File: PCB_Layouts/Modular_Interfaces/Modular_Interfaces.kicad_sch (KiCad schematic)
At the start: 38 parts, among them J1 RJ45_LED, J10 Conn_01x10_Socket, J11 Conn_01x03_Socket, J12 Conn_01x10_Socket, J13 Conn_01x10_Socket, J14 Conn_01x04_Socket, J15 Conn_01x10_Socket, J16 Conn_01x10_Socket, J2 Conn_01x10_Socket, J3 Conn_01x10_Socket, J4 USB_A, J5 Conn_01x10_Socket, J6 Conn_01x10_Socket, J7 USB_A, J8 USB_A, J9 Conn_01x10_Socket, U1 ENC28J60x-SS, Y1 25MHz

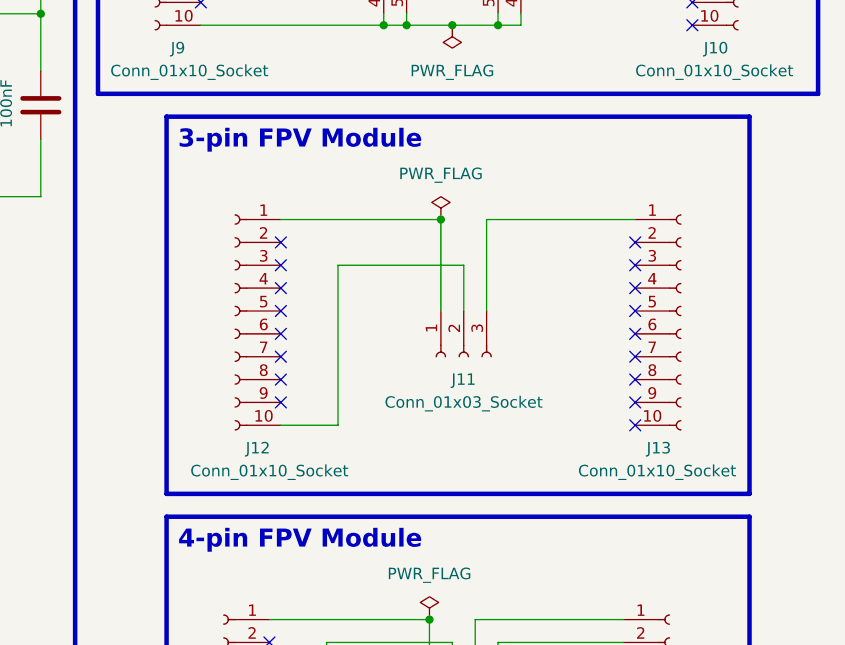
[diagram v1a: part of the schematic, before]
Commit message: Adding Modular Interfaces No GigE module and quote
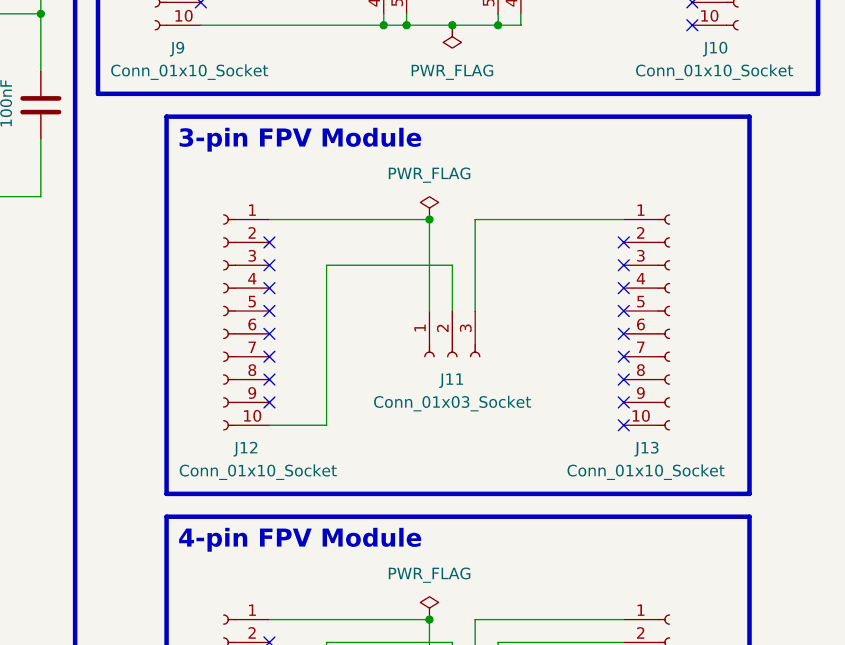
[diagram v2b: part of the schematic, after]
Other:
- title: Modular Interface for Bitcraze Crazyflie 2.0 -> Modular Interfaces for Bitcraze Crazyflie 2.0
- moved on the sheet: J11, J12, J13
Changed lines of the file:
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@@
   (paper "User" 262.992 227.99)
   (title_block
-    (title "Modular Interface for Bitcraze Crazyflie 2.0")
+    (title "Modular Interfaces for Bitcraze Crazyflie 2.0")
     (date "2023-10-04")
     (company "Jose Ignacio Granados Marín")
@@
   (junction (at 24.13 83.82) (diameter 0) (color 0 0 0 0)
   )
-  (junction (at 207.01 106.68) (diameter 0) (color 0 0 0 0)
+  (junction (at 205.74 106.68) (diameter 0) (color 0 0 0 0)
   )
   (junction (at 142.24 104.14) (diameter 0) (color 0 0 0 0)
@@
   )
   (no_connect (at 227.33 173.99))
-  (no_connect (at 228.6 129.54))
+  (no_connect (at 227.33 129.54))
   (no_connect (at 68.58 44.45))
   (no_connect (at 187.96 171.45))
   (no_connect (at 76.2 168.91))
   (no_connect (at 227.33 171.45))
-  (no_connect (at 189.23 124.46))
+  (no_connect (at 187.96 124.46))
   (no_connect (at 187.96 39.37))
   (no_connect (at 227.33 39.37))
-  (no_connect (at 228.6 121.92))
+  (no_connect (at 227.33 121.92))
   (no_connect (at 68.58 34.29))
   (no_connect (at 48.26 24.13))
   (no_connect (at 180.34 80.01))
   (no_connect (at 227.33 41.91))
-  (no_connect (at 189.23 114.3))
-  (no_connect (at 228.6 114.3))
+  (no_connect (at 187.96 114.3))
+  (no_connect (at 227.33 114.3))
   (no_connect (at 68.58 39.37))
   (no_connect (at 187.96 168.91))
   (no_connect (at 227.33 29.21))
   (no_connect (at 234.95 74.93))
-  (no_connect (at 228.6 109.22))
+  (no_connect (at 227.33 109.22))
   (no_connect (at 180.34 69.85))
   (no_connect (at 187.96 153.67))
@@
   (no_connect (at 68.58 104.14))
   (no_connect (at 187.96 41.91))
-  (no_connect (at 189.23 127))
+  (no_connect (at 187.96 127))
   (no_connect (at 76.2 161.29))
   (no_connect (at 234.95 85.09))
@@
   (no_connect (at 227.33 163.83))
   (no_connect (at 68.58 24.13))
-  (no_connect (at 189.23 116.84))
+  (no_connect (at 187.96 116.84))
   (no_connect (at 76.2 166.37))
   (no_connect (at 234.95 77.47))
@@
   (no_connect (at 227.33 36.83))
   (no_connect (at 234.95 67.31))
-  (no_connect (at 228.6 127))
+  (no_connect (at 227.33 127))
   (no_connect (at 68.58 83.82))
   (no_connect (at 227.33 31.75))
-  (no_connect (at 228.6 124.46))
+  (no_connect (at 227.33 124.46))
   (no_connect (at 48.26 41.91))
   (no_connect (at 227.33 26.67))
   (no_connect (at 187.96 24.13))
   (no_connect (at 227.33 44.45))
-  (no_connect (at 228.6 119.38))
+  (no_connect (at 227.33 119.38))
   (no_connect (at 180.34 77.47))
   (no_connect (at 187.96 163.83))
@@
   (no_connect (at 187.96 29.21))
   (no_connect (at 187.96 161.29))
-  (no_connect (at 228.6 116.84))
+  (no_connect (at 227.33 116.84))
   (no_connect (at 187.96 36.83))
-  (no_connect (at 189.23 111.76))
+  (no_connect (at 187.96 111.76))
   (no_connect (at 180.34 72.39))
   (no_connect (at 68.58 36.83))
   (no_connect (at 227.33 161.29))
-  (no_connect (at 189.23 119.38))
-  (no_connect (at 228.6 111.76))
+  (no_connect (at 187.96 119.38))
+  (no_connect (at 227.33 111.76))
   (no_connect (at 68.58 21.59))
   (no_connect (at 187.96 26.67))
@@
   (no_connect (at 180.34 82.55))
   (no_connect (at 187.96 34.29))
-  (no_connect (at 189.23 109.22))
-  (no_connect (at 189.23 121.92))
+  (no_connect (at 187.96 109.22))
+  (no_connect (at 187.96 121.92))
   (no_connect (at 48.26 31.75))
   (no_connect (at 227.33 156.21))
@@
     (stroke (width 0) (type default))
   )
-  (wire (pts (xy 207.01 106.68) (xy 189.23 106.68))
+  (wire (pts (xy 205.74 106.68) (xy 187.96 106.68))
     (stroke (width 0) (type default))
   )
@@
     (stroke (width 0) (type default))
   )
-  (wire (pts (xy 212.09 106.68) (xy 228.6 106.68))
+  (wire (pts (xy 210.82 106.68) (xy 227.33 106.68))
     (stroke (width 0) (type default))
   )
@@
     (stroke (width 0) (type default))
   )
-  (wire (pts (xy 195.58 129.54) (xy 189.23 129.54))
+  (wire (pts (xy 194.31 129.54) (xy 187.96 129.54))
     (stroke (width 0) (type default))
   )
@@
     (stroke (width 0) (type default))
   )
-  (wire (pts (xy 207.01 116.84) (xy 207.01 106.68))
+  (wire (pts (xy 205.74 116.84) (xy 205.74 106.68))
     (stroke (width 0) (type default))
   )
@@
     (stroke (width 0) (type default))
   )
-  (wire (pts (xy 212.09 116.84) (xy 212.09 106.68))
+  (wire (pts (xy 210.82 116.84) (xy 210.82 106.68))
     (stroke (width 0) (type default))
   )
@@
     (stroke (width 0) (type default))
   )
-  (wire (pts (xy 209.55 116.84) (xy 209.55 111.76))
+  (wire (pts (xy 208.28 116.84) (xy 208.28 111.76))
     (stroke (width 0) (type default))
   )
@@
     (stroke (width 0) (type default))
   )
-  (wire (pts (xy 209.55 111.76) (xy 195.58 111.76))
+  (wire (pts (xy 208.28 111.76) (xy 194.31 111.76))
     (stroke (width 0) (type default))
   )
@@
     (stroke (width 0) (type default))
   )
-  (wire (pts (xy 195.58 111.76) (xy 195.58 129.54))
+  (wire (pts (xy 194.31 111.76) (xy 194.31 129.54))
     (stroke (width 0) (type default))
   )
@@
     )
   )
-  (symbol (lib_id "Connector:Conn_01x03_Socket") (at 209.55 121.92 90) (mirror x) (unit 1)
-    (in_bom yes) (on_board yes) (dnp no)
-    (property "Reference" "J11" (at 209.55 124.46 90)
-      (effects (font (size 1.27 1.27)))
-    )
-    (property "Value" "Conn_01x03_Socket" (at 209.55 127 90)
-      (effects (font (size 1.27 1.27)))
-    )
-    (property "Footprint" "Connector_JST:JST_XH_B3B-XH-A_1x03_P2.50mm_Vertical" (at 209.55 121.92 0)
-      (effects (font (size 1.27 1.27)) hide)
-    )
-    (property "Datasheet" "~" (at 209.55 121.92 0)
+  (symbol (lib_id "Connector:Conn_01x03_Socket") (at 208.28 121.92 90) (mirror x) (unit 1)
+    (in_bom yes) (on_board yes) (dnp no)
+    (property "Reference" "J11" (at 208.28 124.46 90)
+      (effects (font (size 1.27 1.27)))
+    )
+    (property "Value" "Conn_01x03_Socket" (at 208.28 127 90)
+      (effects (font (size 1.27 1.27)))
+    )
+    (property "Footprint" "Connector_JST:JST_XH_B3B-XH-A_1x03_P2.50mm_Vertical" (at 208.28 121.92 0)
+      (effects (font (size 1.27 1.27)) hide)
+    )
+    (property "Datasheet" "~" (at 208.28 121.92 0)
       (effects (font (size 1.27 1.27)) hide)
     )
@@
     )
   )
-  (symbol (lib_id "Connector:Conn_01x10_Socket") (at 184.15 116.84 0) (mirror y) (unit 1)
-    (in_bom yes) (on_board yes) (dnp no)
-    (property "Reference" "J12" (at 186.69 132.08 0)
-      (effects (font (size 1.27 1.27)))
-    )
-    (property "Value" "Conn_01x10_Socket" (at 187.96 134.62 0)
-      (effects (font (size 1.27 1.27)))
-    )
-    (property "Footprint" "Connector_PinSocket_2.00mm:PinSocket_1x10_P2.00mm_Vertical" (at 184.15 116.84 0)
-      (effects (font (size 1.27 1.27)) hide)
-    )
-    (property "Datasheet" "~" (at 184.15 116.84 0)
+  (symbol (lib_id "Connector:Conn_01x10_Socket") (at 182.88 116.84 0) (mirror y) (unit 1)
+    (in_bom yes) (on_board yes) (dnp no)
+    (property "Reference" "J12" (at 185.42 132.08 0)
+      (effects (font (size 1.27 1.27)))
+    )
+    (property "Value" "Conn_01x10_Socket" (at 186.69 134.62 0)
+      (effects (font (size 1.27 1.27)))
+    )
+    (property "Footprint" "Connector_PinSocket_2.00mm:PinSocket_1x10_P2.00mm_Vertical" (at 182.88 116.84 0)
+      (effects (font (size 1.27 1.27)) hide)
+    )
+    (property "Datasheet" "~" (at 182.88 116.84 0)
       (effects (font (size 1.27 1.27)) hide)
     )
@@
     )
   )
-  (symbol (lib_id "power:PWR_FLAG") (at 207.01 106.68 0) (unit 1)
+  (symbol (lib_id "power:PWR_FLAG") (at 205.74 106.68 0) (unit 1)
     (in_bom yes) (on_board yes) (dnp no) (fields_autoplaced)
-    (property "Reference" "#FLG07" (at 207.01 104.775 0)
-      (effects (font (size 1.27 1.27)) hide)
-    )
-    (property "Value" "PWR_FLAG" (at 207.01 101.6 0)
-      (effects (font (size 1.27 1.27)))
-    )
-    (property "Footprint" "" (at 207.01 106.68 0)
-      (effects (font (size 1.27 1.27)) hide)
-    )
-    (property "Datasheet" "~" (at 207.01 106.68 0)
+    (property "Reference" "#FLG07" (at 205.74 104.775 0)
+      (effects (font (size 1.27 1.27)) hide)
+    )
+    (property "Value" "PWR_FLAG" (at 205.74 101.6 0)
+      (effects (font (size 1.27 1.27)))
+    )
+    (property "Footprint" "" (at 205.74 106.68 0)
+      (effects (font (size 1.27 1.27)) hide)
+    )
+    (property "Datasheet" "~" (at 205.74 106.68 0)
       (effects (font (size 1.27 1.27)) hide)
     )
@@
     )
   )
-  (symbol (lib_id "Connector:Conn_01x10_Socket") (at 233.68 116.84 0) (unit 1)
-    (in_bom yes) (on_board yes) (dnp no)
-    (property "Reference" "J13" (at 229.87 132.08 0)
-      (effects (font (size 1.27 1.27)) (justify left))
-    )
-    (property "Value" "Conn_01x10_Socket" (at 222.25 134.62 0)
-      (effects (font (size 1.27 1.27)) (justify left))
-    )
-    (property "Footprint" "Connector_PinSocket_2.00mm:PinSocket_1x10_P2.00mm_Vertical" (at 233.68 116.84 0)
-      (effects (font (size 1.27 1.27)) hide)
-    )
-    (property "Datasheet" "~" (at 233.68 116.84 0)
-      (effects (font (size 1.27 1.27)) hide)
-    )
+  (symbol (lib_id "Connector:Conn_01x10_Socket") (at 232.41 116.84 0) (unit 1)
+    (in_bom yes) (on_board yes) (dnp no)
+    (property "Reference" "J13" (at 228.6 132.08 0)
+      (effects (font (size 1.27 1.27)) (justify left))
+    )
+    (property "Value" "Conn_01x10_Socket" (at 220.98 134.62 0)
+      (effects (font (size 1.27 1.27)) (justify left))
+    )
+    (property "Footprint" "Connector_PinSocket_2.00mm:PinSocket_1x10_P2.00mm_Vertical" (at 232.41 116.84 0)
+      (effects (font (size 1.27 1.27)) hide)
+    )
+    (property "Datasheet" "~" (at 232.41 116.84 0)
+      (effects (font (size 1.27 1.27)) hide)
+    )
